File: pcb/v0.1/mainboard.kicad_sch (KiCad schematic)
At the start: 4 parts, among them J11 USB_C_Receptacle_USB2.0

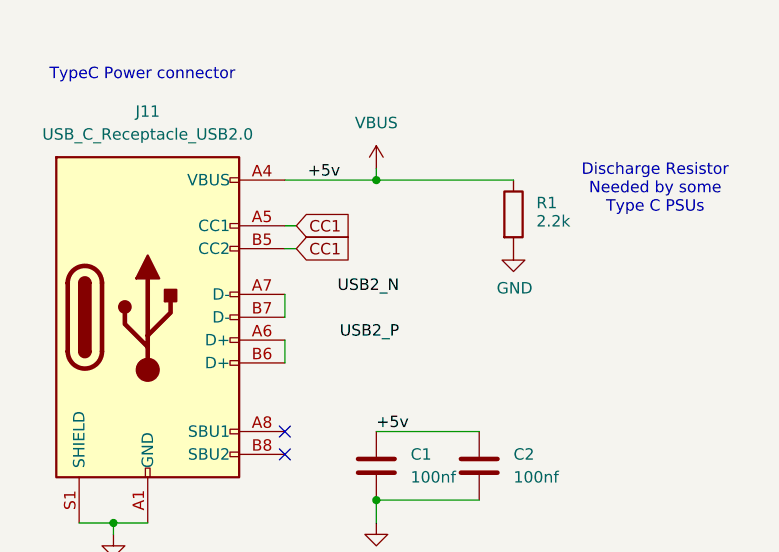
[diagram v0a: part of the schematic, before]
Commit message: Add co processor as its own sub page
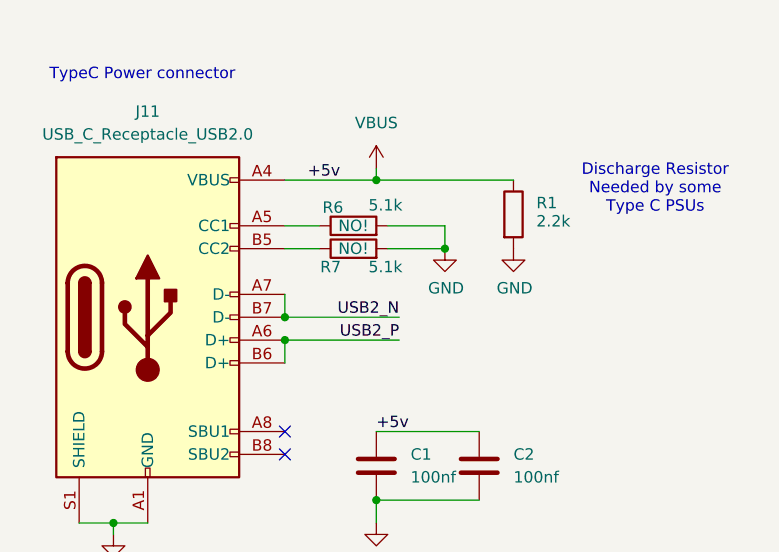
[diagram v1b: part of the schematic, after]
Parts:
- added R6, R7: 5.1k, Resistor_SMD:R_0603_1608Metric, symbol TH-1-CC:R_5.1k
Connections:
- net GND: now also R6.2, R7.2
- net USB2_N: now also J11.A7 (D-), J11.B7 (D-)
- net USB2_P: now also J11.A6 (D+), J11.B6 (D+)
- net CC1: no longer names the net of J11.A5 (CC1)
- net CC1: now also R6.1; no longer J11.B5 (CC2)
- new net: J11.B5 (CC2), R7.1

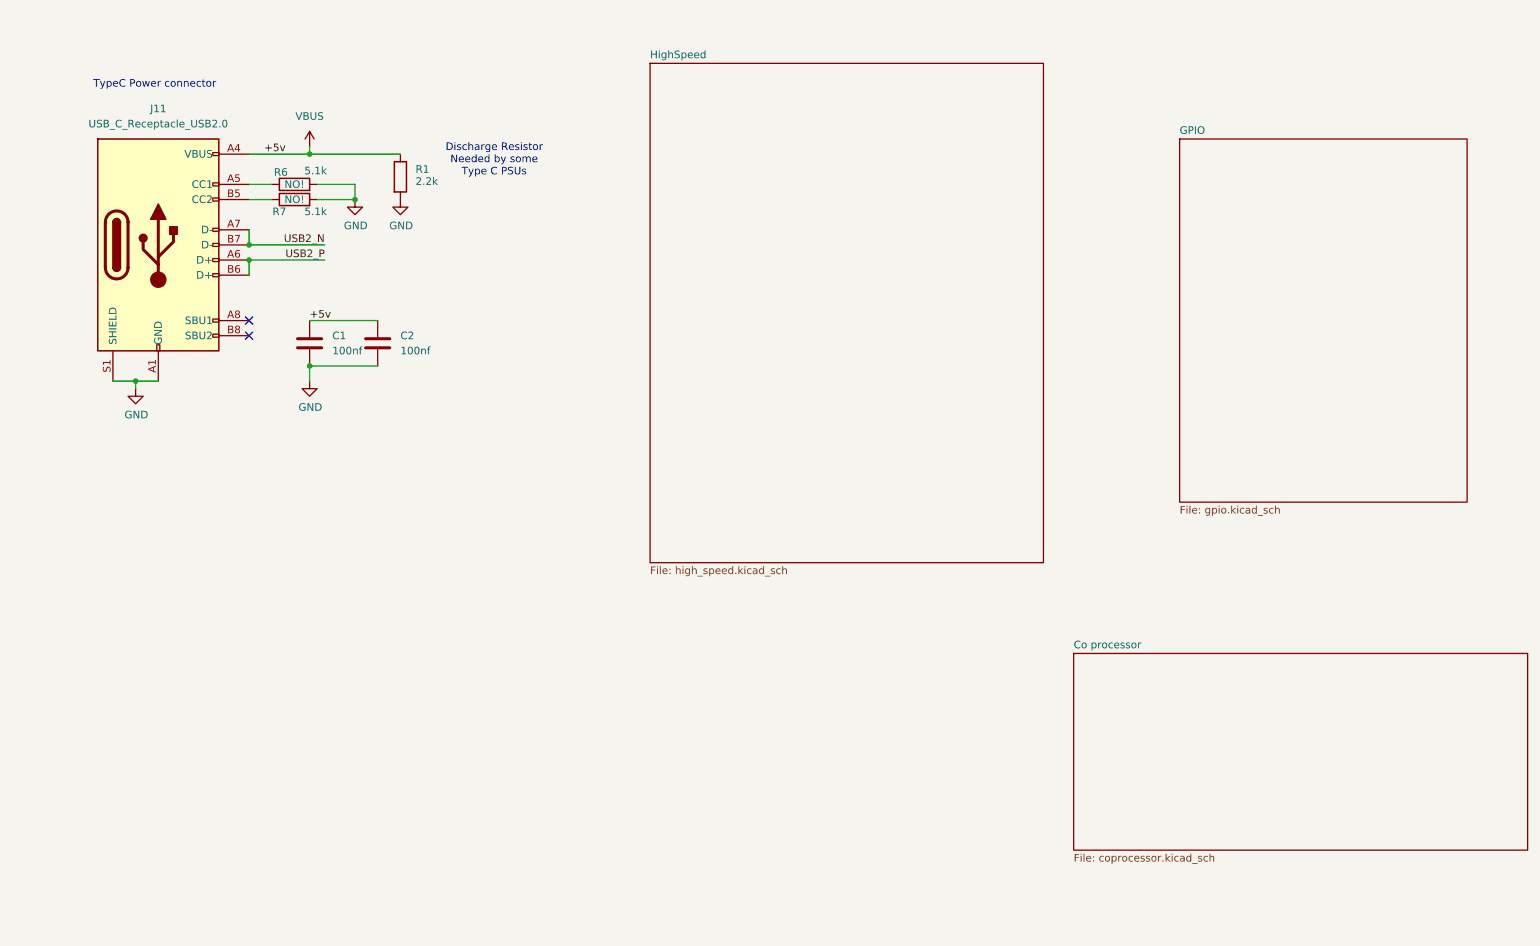
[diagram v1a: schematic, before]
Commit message: Add IR subsystem to schematic + clean up layout
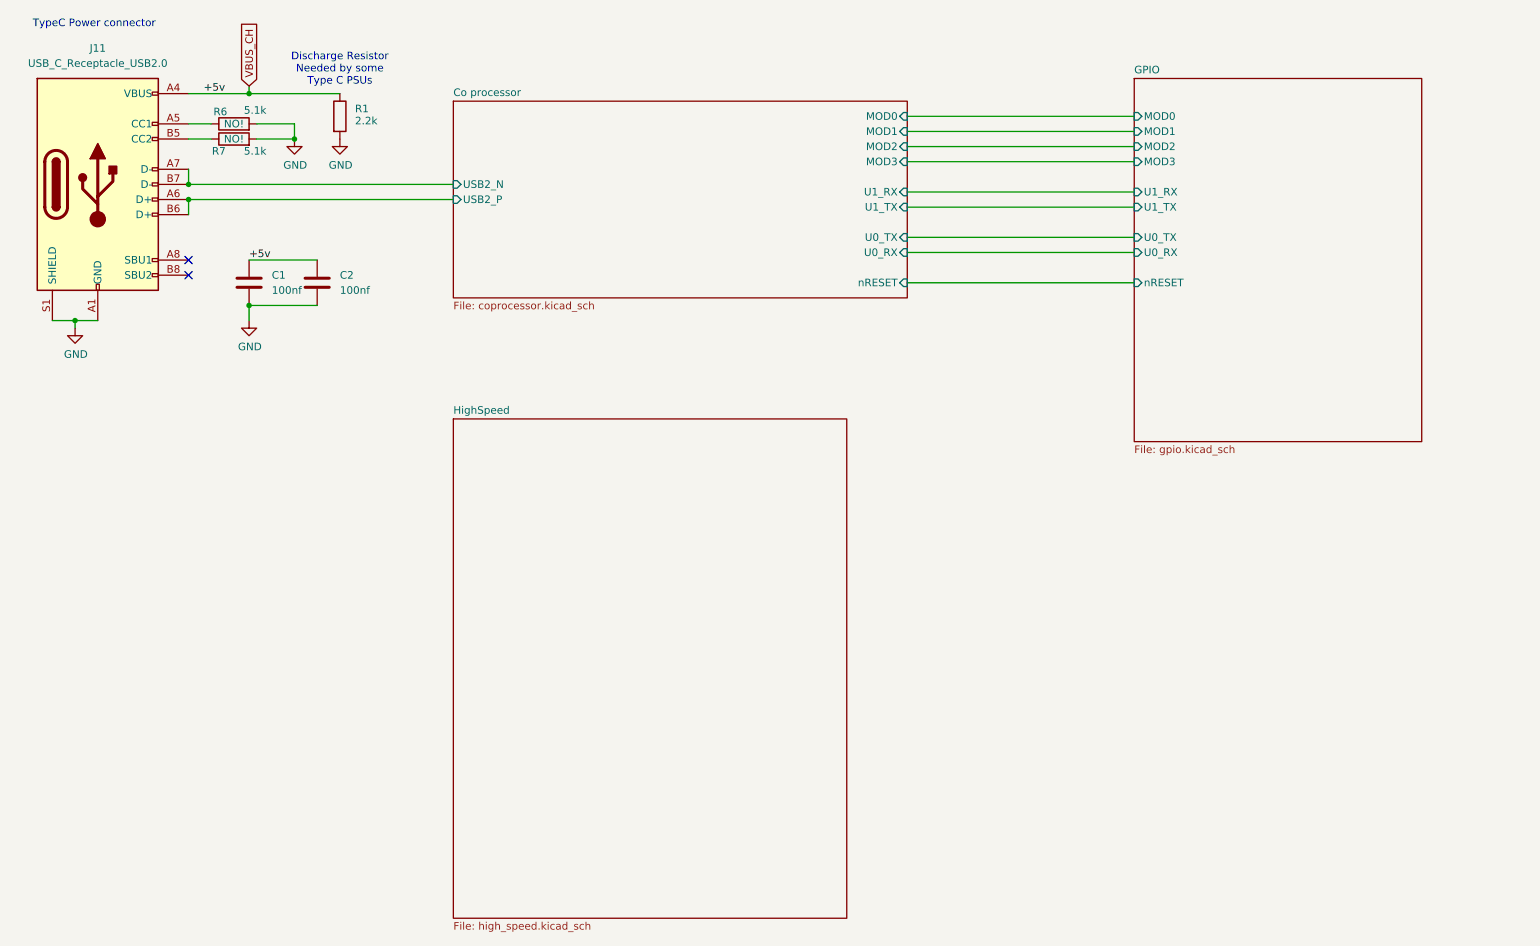
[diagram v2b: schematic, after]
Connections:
- net USB2_N renamed Co processor/USB2_N
- net USB2_P renamed Co processor/USB2_P
- net VBUS renamed VBUS_CH
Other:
- sheet Co processor ports: added MOD0, MOD1, MOD2, MOD3, U0_RX, U0_TX, U1_RX, U1_TX, USB2_N, USB2_P, nRESET; removed none
- sheet GPIO ports: added MOD0, MOD1, MOD2, MOD3, U0_RX, U0_TX, U1_RX, U1_TX, nRESET; removed none
- company: (none) -> Teahaz Computer
- title: (none) -> TH-1 Mainboard devkit
- moved on the sheet: C1, C2, J11, R1, R6, R7

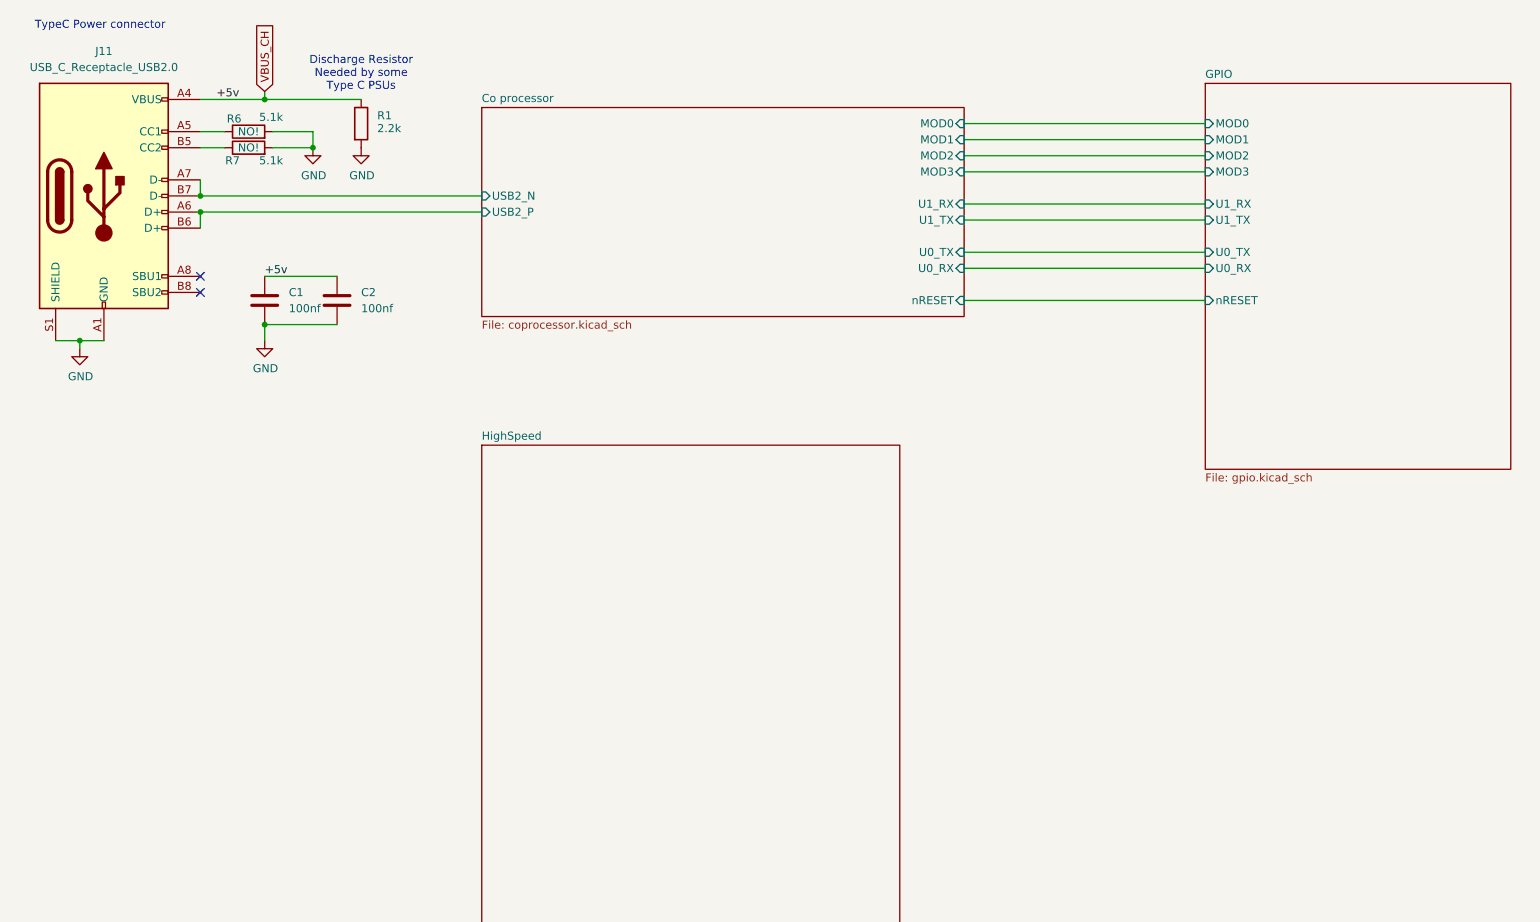
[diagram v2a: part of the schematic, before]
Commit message: Continue mainboard schematic work
- Updated pins connecting to i2c and the co processor based on breadboard
testing.
- Added SD card reader
- Added power switch
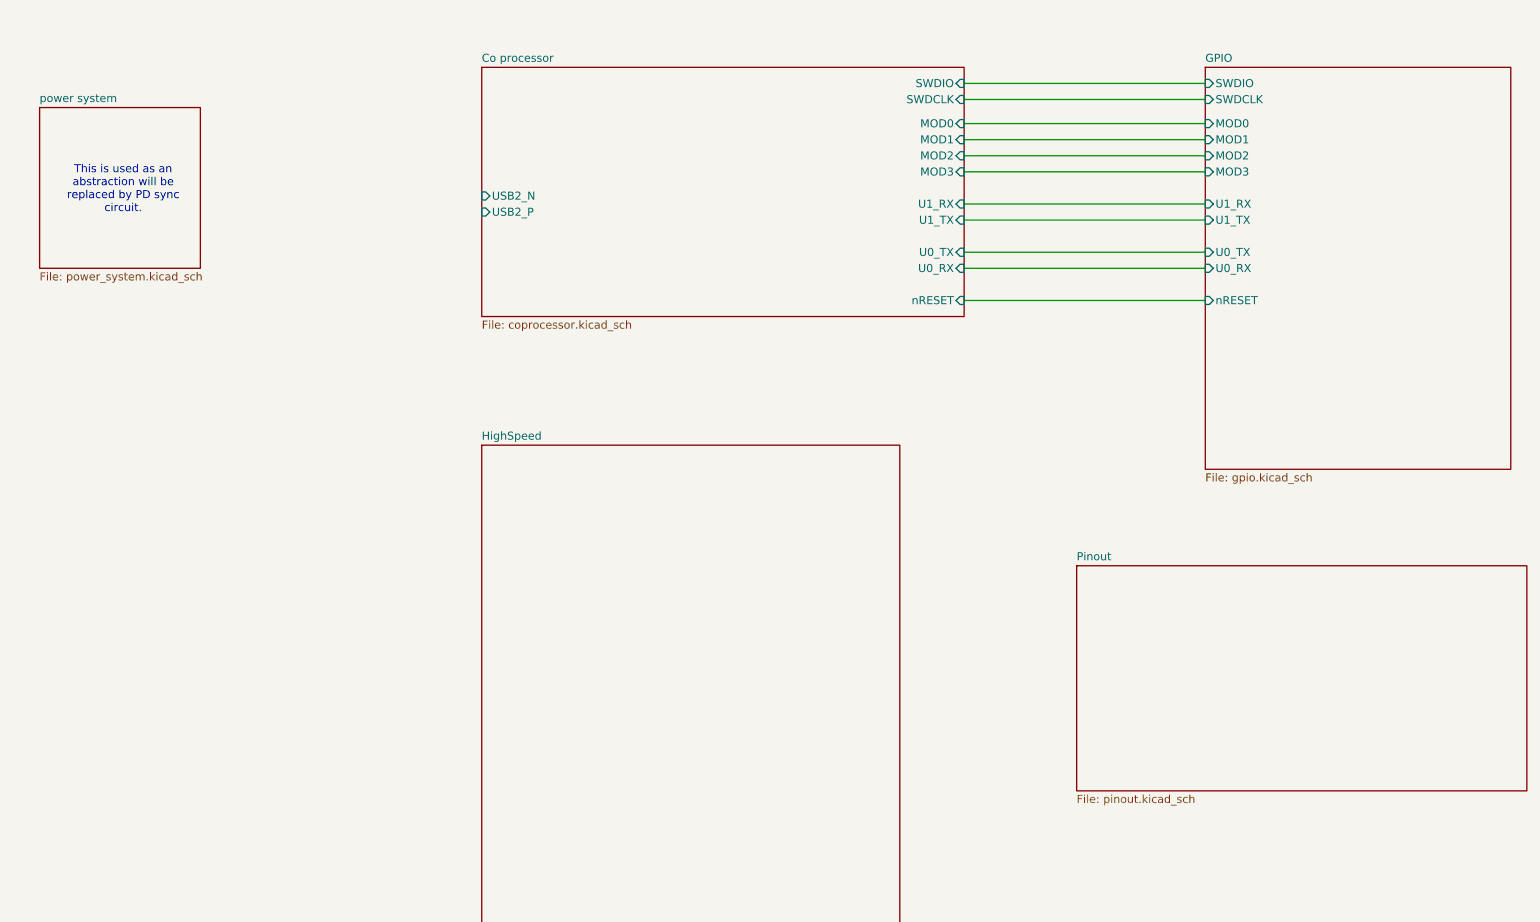
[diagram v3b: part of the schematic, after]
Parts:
- removed C1, C2: 100nf, Capacitor_SMD:C_0603_1608Metric, symbol TH-1-CC:C_100nf
- removed J11: USB_C_Receptacle_USB2.0, Connector_USB:USB_C_Receptacle_GCT_USB4105-xx-A_16P_TopMnt_Horizontal, symbol Connector:USB_C_Receptacle_USB2.0_16P
- removed R1: 2.2k, Resistor_SMD:R_0603_1608Metric, symbol TH-1-CC:R_2.2k
- removed R6, R7: 5.1k, Resistor_SMD:R_0603_1608Metric, symbol TH-1-CC:R_5.1k
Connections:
- no-connect marks 2 -> 0
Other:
- added sheet Pinout (pinout.kicad_sch)
- added sheet power system (power_system.kicad_sch)
- sheet Co processor ports: added SWDCLK, SWDIO; removed none
- sheet GPIO ports: added SWDCLK, SWDIO; removed none
- note added: "This is used as an abstraction will be replaced by PD sync circuit."
- note removed: "Discharge Resistor Needed by some Type C PSUs"
- note removed: "TypeC Power connector"
